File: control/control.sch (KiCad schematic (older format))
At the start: 153 parts, among them IC1 TJA1040, IC2 DNP MAX481CSA, IC3 ST232BD, IC4 ATMEGA128-A, IC5 ST232BD, IC6 FT232RL, J4 POWER, P1 SENSOR, P10 DB9, P11 USB_B, P12 USB_OTG, P13 DB9, P2 I2C0, P3 I2C1, P4 I2C2, P5 COIN, P6 BILL, P7 ISP, P8 12V, P9 5V, X1 16MHz

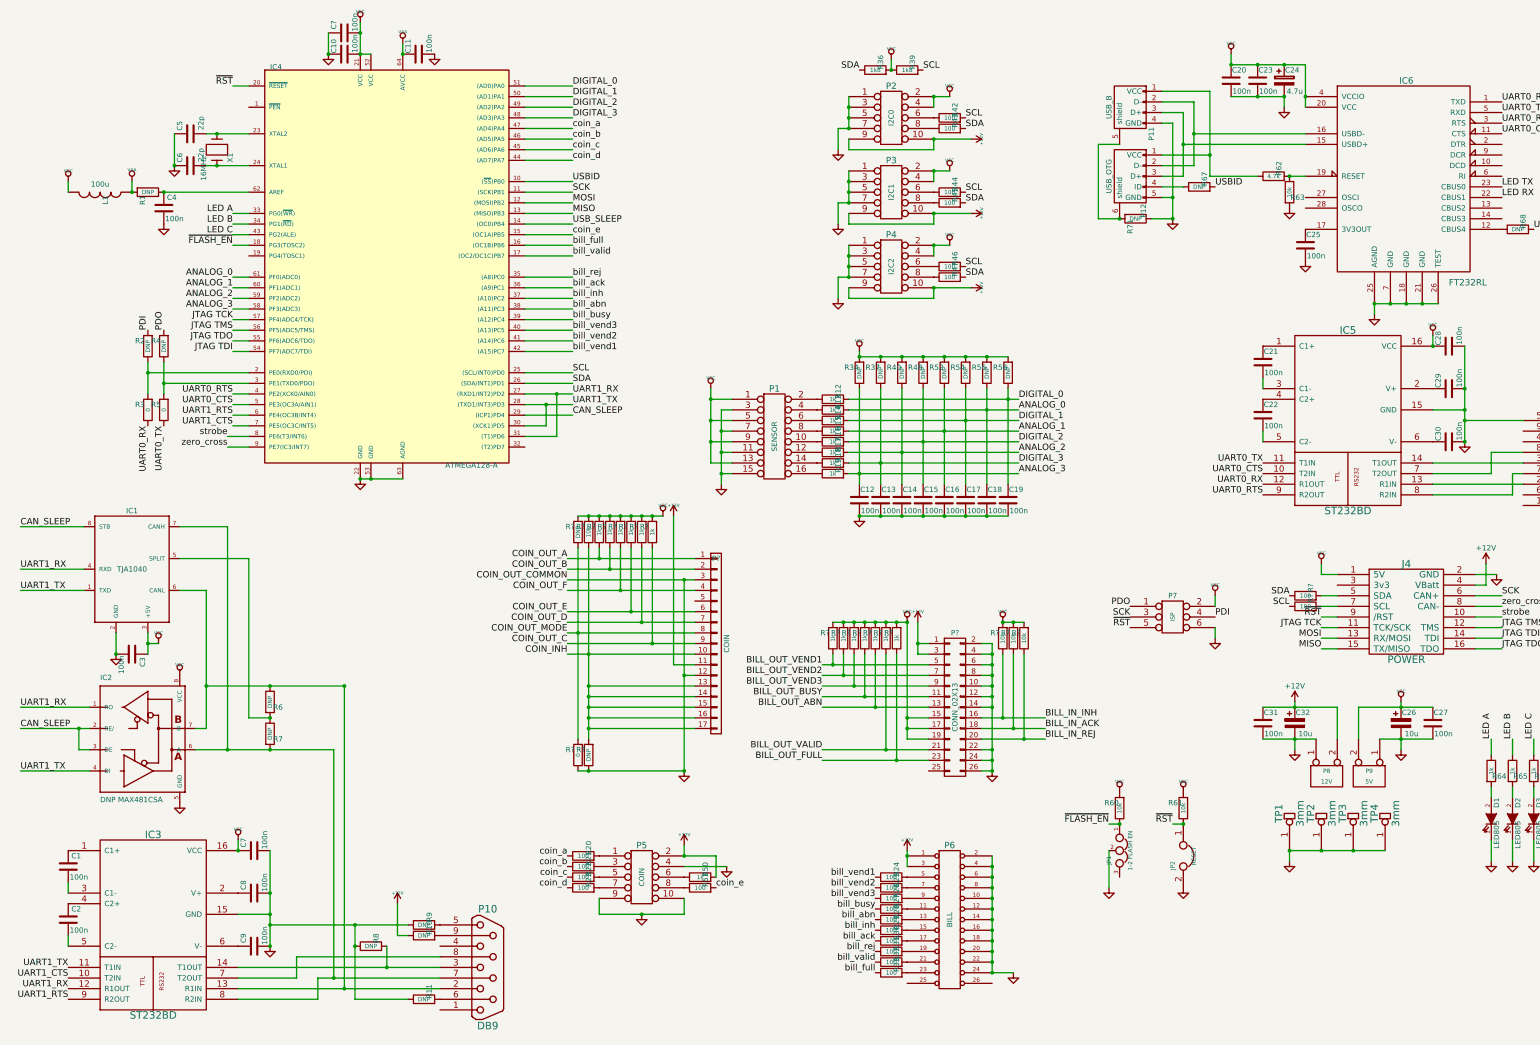
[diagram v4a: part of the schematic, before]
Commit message: Removed old coin and banknote connection block in schematic, rewired MCU for new block
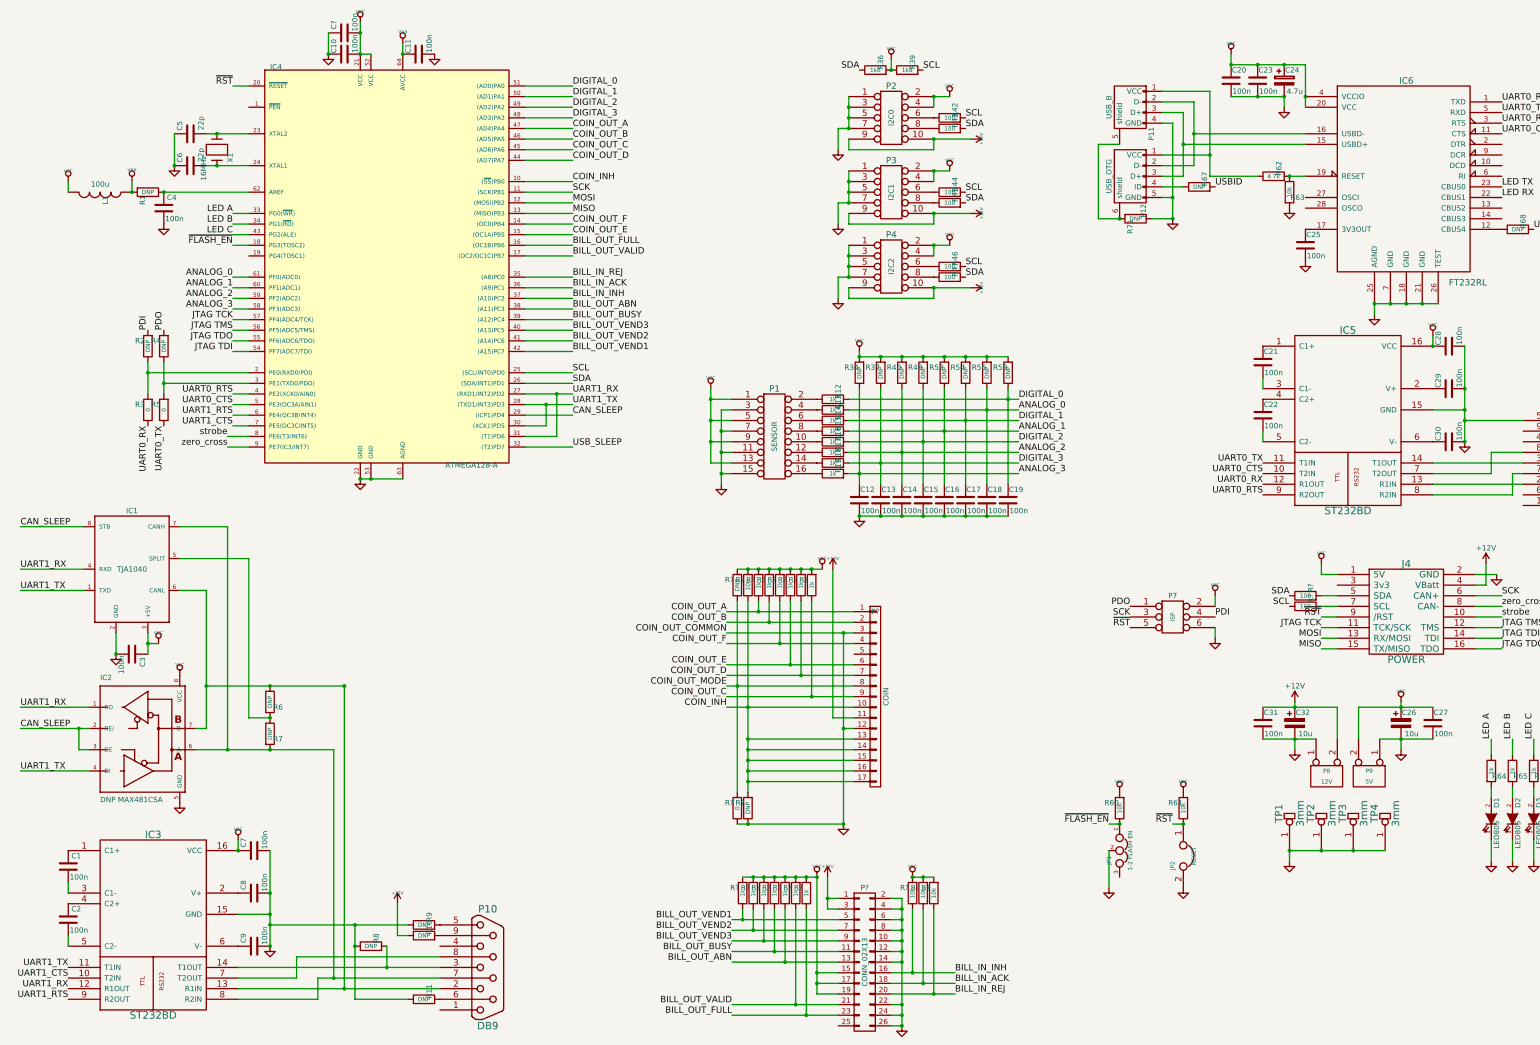
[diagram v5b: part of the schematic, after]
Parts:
- removed P5: COIN, Pin_Headers:Pin_Header_Straight_2x05, symbol CONN_5X2
- removed P6: BILL, Pin_Headers:Pin_Header_Straight_2x13, symbol CONN_13X2
- removed R20, R21, R22, R23, R24, R25, R26, R27, R28, R29, R30, R31, R32, R33, R51: 100, Resistors_SMD:R_0805_HandSoldering, symbol R
- removed R50: 1k, Resistors_SMD:R_0805_HandSoldering, symbol R
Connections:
- net bill_abn is gone; now on net BILL_OUT_ABN: IC4.38 ((A11)PC3)
- net bill_ack is gone; now on net BILL_IN_ACK: IC4.36 ((A9)PC1)
- net bill_busy is gone; now on net BILL_OUT_BUSY: IC4.39 ((A12)PC4)
- net bill_full is gone; now on net BILL_OUT_FULL: IC4.16 ((OC1B)PB6)
- net bill_inh is gone; now on net BILL_IN_INH: IC4.37 ((A10)PC2)
- net bill_rej is gone; now on net BILL_IN_REJ: IC4.35 ((A8)PC0)
- net bill_valid is gone; now on net BILL_OUT_VALID: IC4.17 ((OC2/OC1C)PB7)
- net bill_vend1 is gone; now on net BILL_OUT_VEND1: IC4.42 ((A15)PC7)
- net bill_vend2 is gone; now on net BILL_OUT_VEND2: IC4.41 ((A14)PC6)
- net bill_vend3 is gone; now on net BILL_OUT_VEND3: IC4.40 ((A13)PC5)
- net coin_a is gone; now on net COIN_OUT_A: IC4.47 ((AD4)PA4)
- net coin_b is gone; now on net COIN_OUT_B: IC4.46 ((AD5)PA5)
- net coin_c is gone; now on net COIN_OUT_C: IC4.45 ((AD6)PA6)
- net coin_d is gone; now on net COIN_OUT_D: IC4.44 ((AD7)PA7)
- net coin_e is gone; now on net COIN_OUT_E: IC4.15 ((OC1A)PB5)
- net COIN_INH: now also IC4.10 ((~SS~)PB0)
- net COIN_OUT_F: now also IC4.14 ((OC0)PB4)
- net USBID: no longer IC4.10 ((~SS~)PB0)
- net USB_SLEEP: now also IC4.32 ((T2)PD7); no longer IC4.14 ((OC0)PB4)
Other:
- moved on the sheet: P?, R?

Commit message: Added optional linear regulator for 5V Vcc. Replaced old connector symbols with current ones from the KiCad library.
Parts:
- added U?: DNP LM2940-N 5V, symbol LM2937
- P1: symbol CONN_8X2 -> CONN_02X08
- P2, P3, P4: symbol CONN_5X2 -> CONN_02X05
- P7: symbol CONN_3X2 -> CONN_02X03
- P8, P9: symbol CONN_2 -> CONN_01X02
- TP1, TP2, TP3, TP4: symbol CONNECTOR -> CONN_01X01
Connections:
- net +12V: now also U?.1 (VI)
- net GND: now also U?.2 (GND)
- net VCC: now also U?.3 (VO); no longer R34.2, R37.2, R40.2, R48.2, R52.2, R54.2, R56.2, R58.2
- new net: R34.2, R37.2, R40.2, R48.2, R52.2, R54.2, R56.2, R58.2
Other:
- moved on the sheet: C26, C27, C31, C32, JP1, JP2, P1, P2, P3, P4, P7, P8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

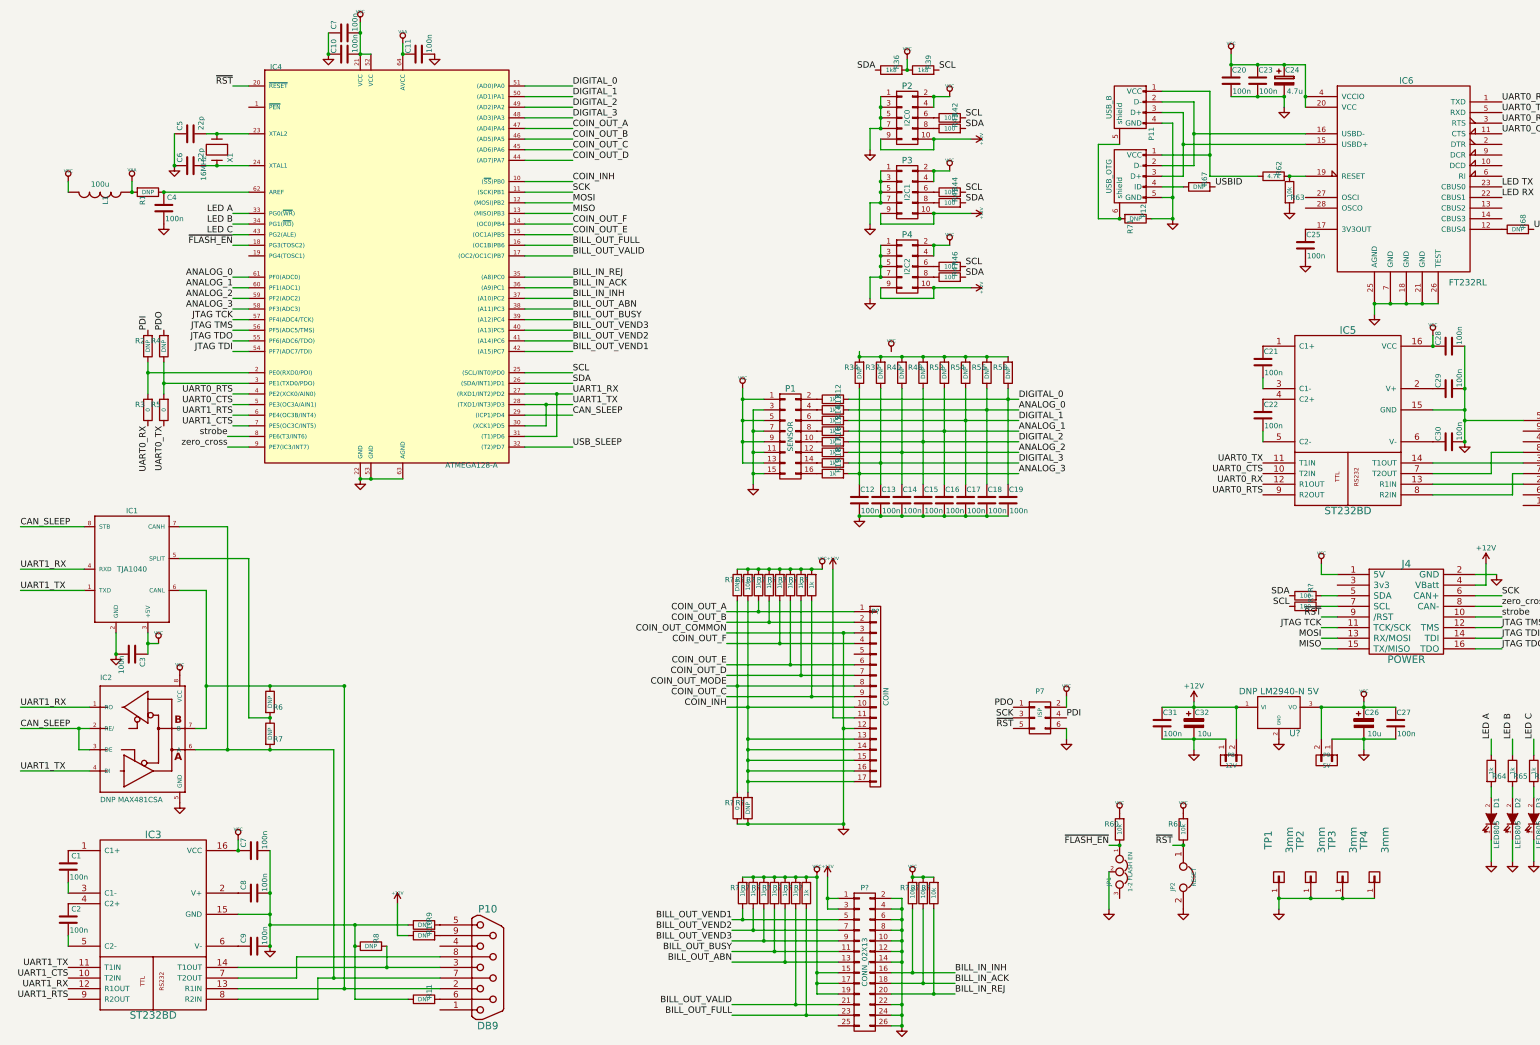
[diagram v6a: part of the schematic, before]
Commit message: Updated layout with new/changed parts
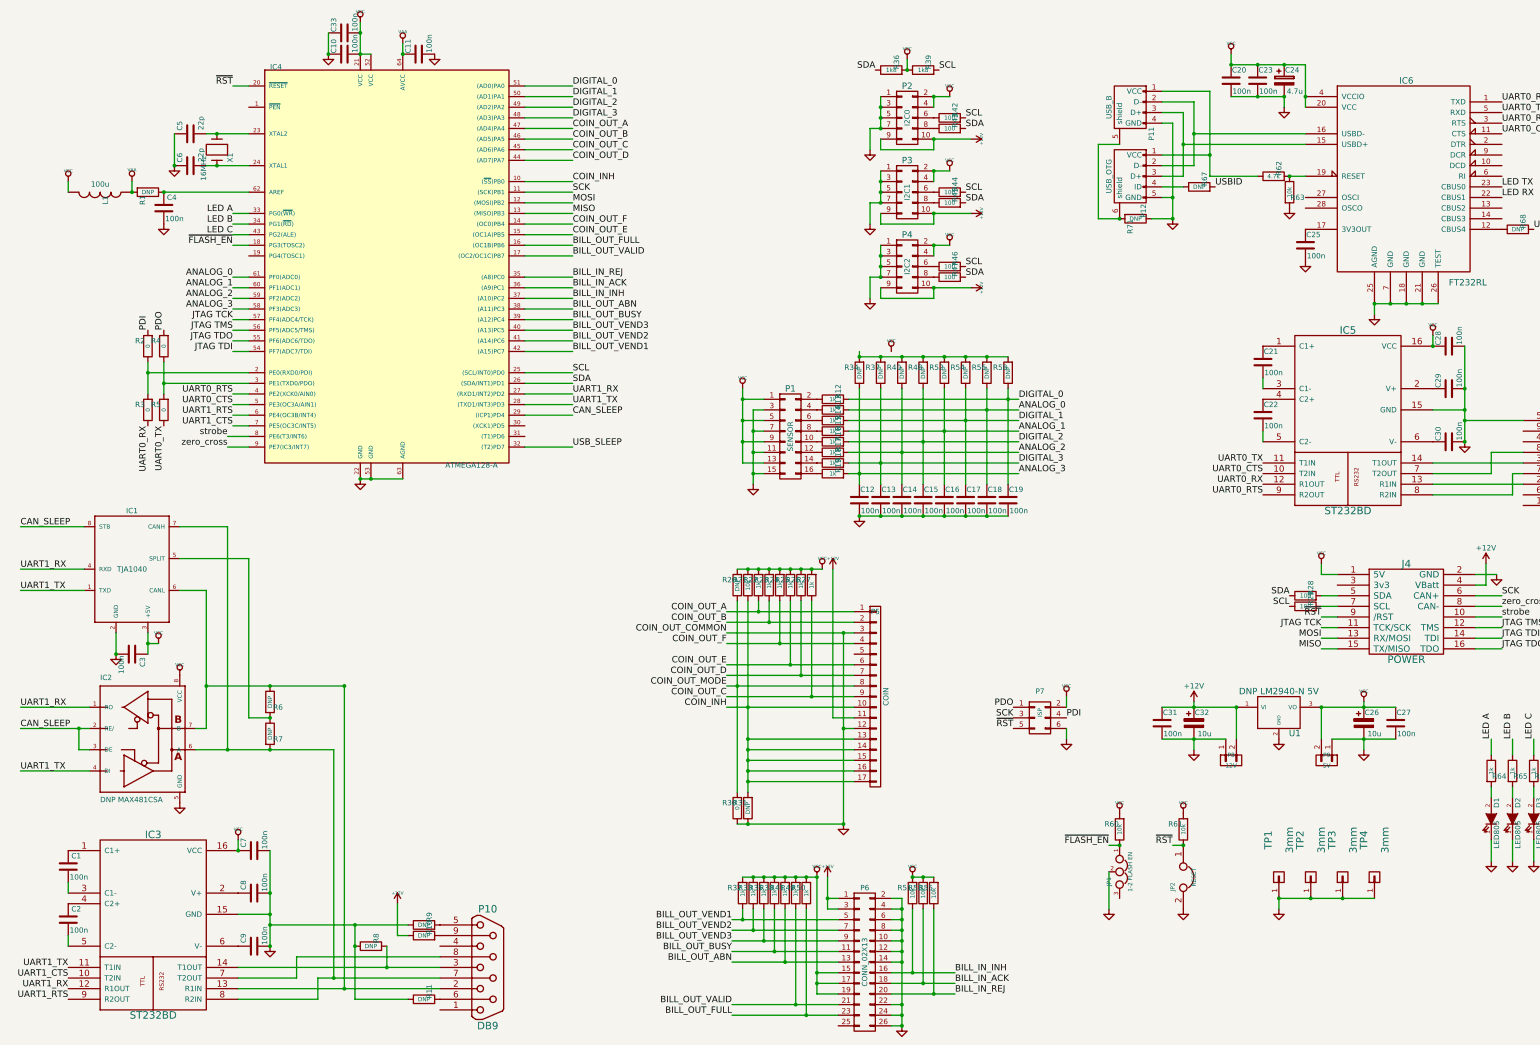
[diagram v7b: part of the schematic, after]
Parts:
- JP2: footprint Pin_Headers:Pin_Header_Straight_1x03 -> Pin_Headers:Pin_Header_Straight_1x02
- P5: renamed from P?; footprint (none) -> Pin_Headers:Pin_Header_Straight_1x17
- P6: renamed from P?; footprint (none) -> Pin_Headers:Pin_Header_Straight_2x13
- R2, R4: value DNP -> 0
- U1: renamed from U?; footprint (none) -> matemat:SOT-223
- gave numbers to parts that had none: 23
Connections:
- net UART1_RX: no longer IC4.31 ((T1)PD6)
- net UART1_TX: no longer IC4.30 ((XCK1)PD5)

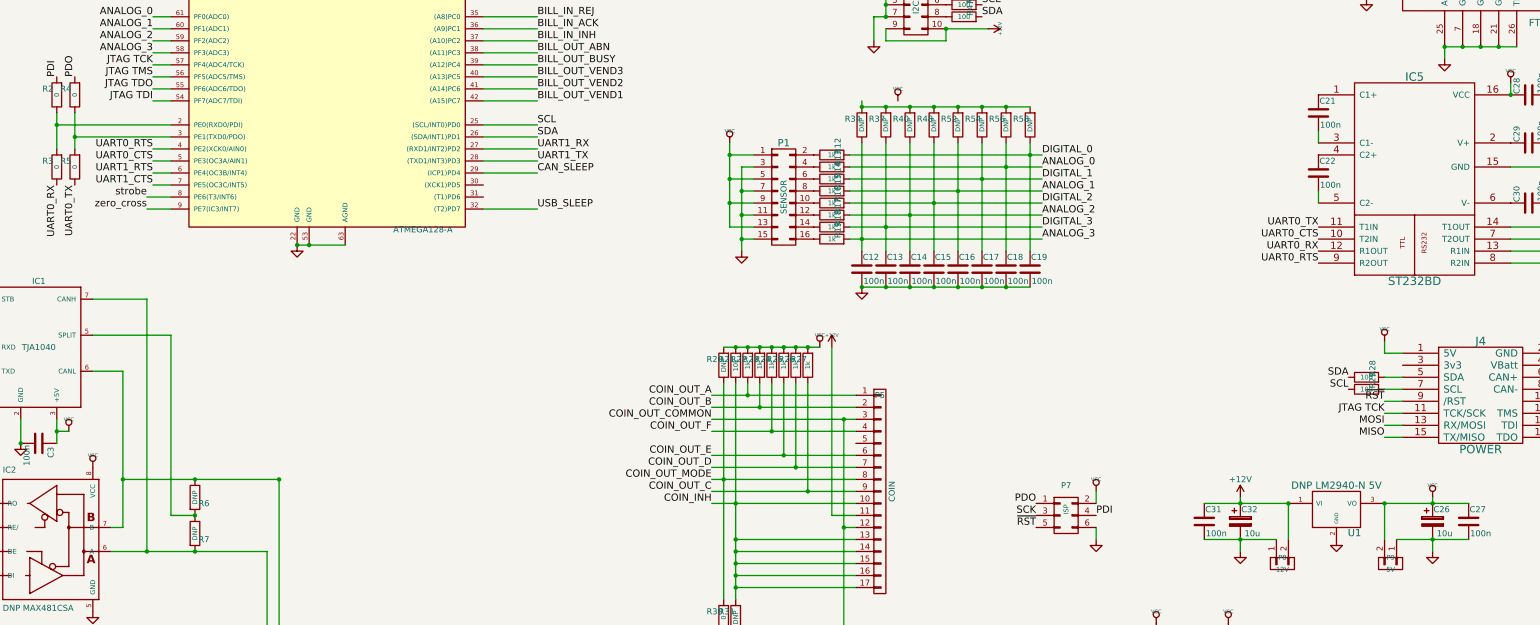
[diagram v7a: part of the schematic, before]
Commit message: WIP control board rewiring to make it smaller
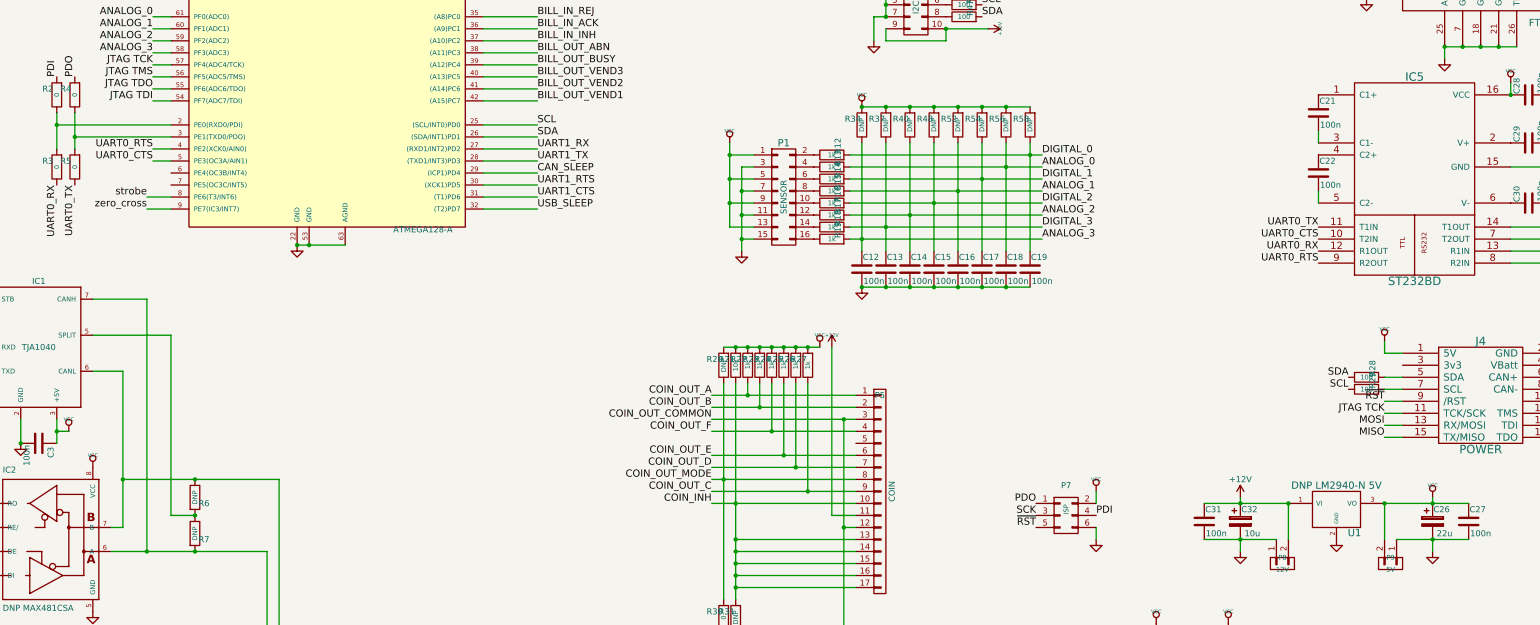
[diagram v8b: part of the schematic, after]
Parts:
- C26: value 10u -> 22u
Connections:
- net UART1_CTS: now also IC4.31 ((T1)PD6); no longer IC4.7 (PE5(OC3C/INT5))
- net UART1_RTS: now also IC4.30 ((XCK1)PD5); no longer IC4.6 (PE4(OC3B/INT4))
- net VCC: now also R34.2, R37.2, R40.2, R48.2, R52.2, R54.2, R56.2, R58.2
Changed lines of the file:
@@
 P 13700 7750
 F 0 "C26" H 13775 7850 50  0000 C CNN
-F 1 "10u" H 13800 7650 50  0000 C CNN
+F 1 "22u" H 13800 7650 50  0000 C CNN
 F 2 "Capacitors_ThroughHole:C_Radial_D5_L11_P2.5" H 13700 7750 60  0001 C CNN
 F 3 "" H 13700 7750 60  0001 C CNN
@@
 Text Label 1500 10050 2    60   ~ 0
 UART1_TX
-Text Label 3050 4850 2    60   ~ 0
+Text Label 6250 4950 0    60   ~ 0
 UART1_RTS
-Text Label 3050 4950 2    60   ~ 0
+Text Label 6250 5050 0    60   ~ 0
 UART1_CTS
 Text Label 3050 3050 2    60   ~ 0
@@
 L VCC #PWR049
 U 1 1 513FD79F
-P 9250 4250
-F 0 "#PWR049" H 9250 4350 30  0001 C CNN
-F 1 "VCC" H 9250 4350 30  0000 C CNN
-F 2 "" H 9250 4250 60  0001 C CNN
-F 3 "" H 9250 4250 60  0001 C CNN
-	1    9250 4250
+P 8950 4300
+F 0 "#PWR049" H 8950 4400 30  0001 C CNN
+F 1 "VCC" H 8950 4400 30  0000 C CNN
+F 2 "" H 8950 4300 60  0001 C CNN
+F 3 "" H 8950 4300 60  0001 C CNN
+	1    8950 4300
 	1    0    0    -1
 $EndComp
@@
 Wire Wire Line
 	8950 4300 10350 4300
-Wire Wire Line
-	8950 4300 8950 4250
 Connection ~ 9150 5800
 Connection ~ 9150 5300
@@
 	3200 2950 3050 2950
 Wire Wire Line
-	3200 4950 3050 4950
-Wire Wire Line
-	3200 4850 3050 4850
-Wire Wire Line
 	9650 3350 9650 3250
 Connection ~ 9150 3450
@@
 Connection ~ 3400 7700
 Connection ~ 2800 7400
-Connection ~ 4100 7400
 Connection ~ 3400 7400
 Wire Wire Line
@@
 Connection ~ 12500 7600
 Connection ~ 13300 7600
+Wire Wire Line
+	6250 4950 5800 4950
+Wire Wire Line
+	5800 5050 6250 5050
 $EndSCHEMATC
